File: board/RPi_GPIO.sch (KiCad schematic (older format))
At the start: 37 parts, among them IC1 ATMEGA328-A, IC2 RFM69HW, J1 RPi_GPIO, P1 FTDI_CONN_01X06, P10 SW_CONN, P11 BATT_IN, P12 CONN_01X01, P2 D4, P3 ADC0, P4 ADC1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

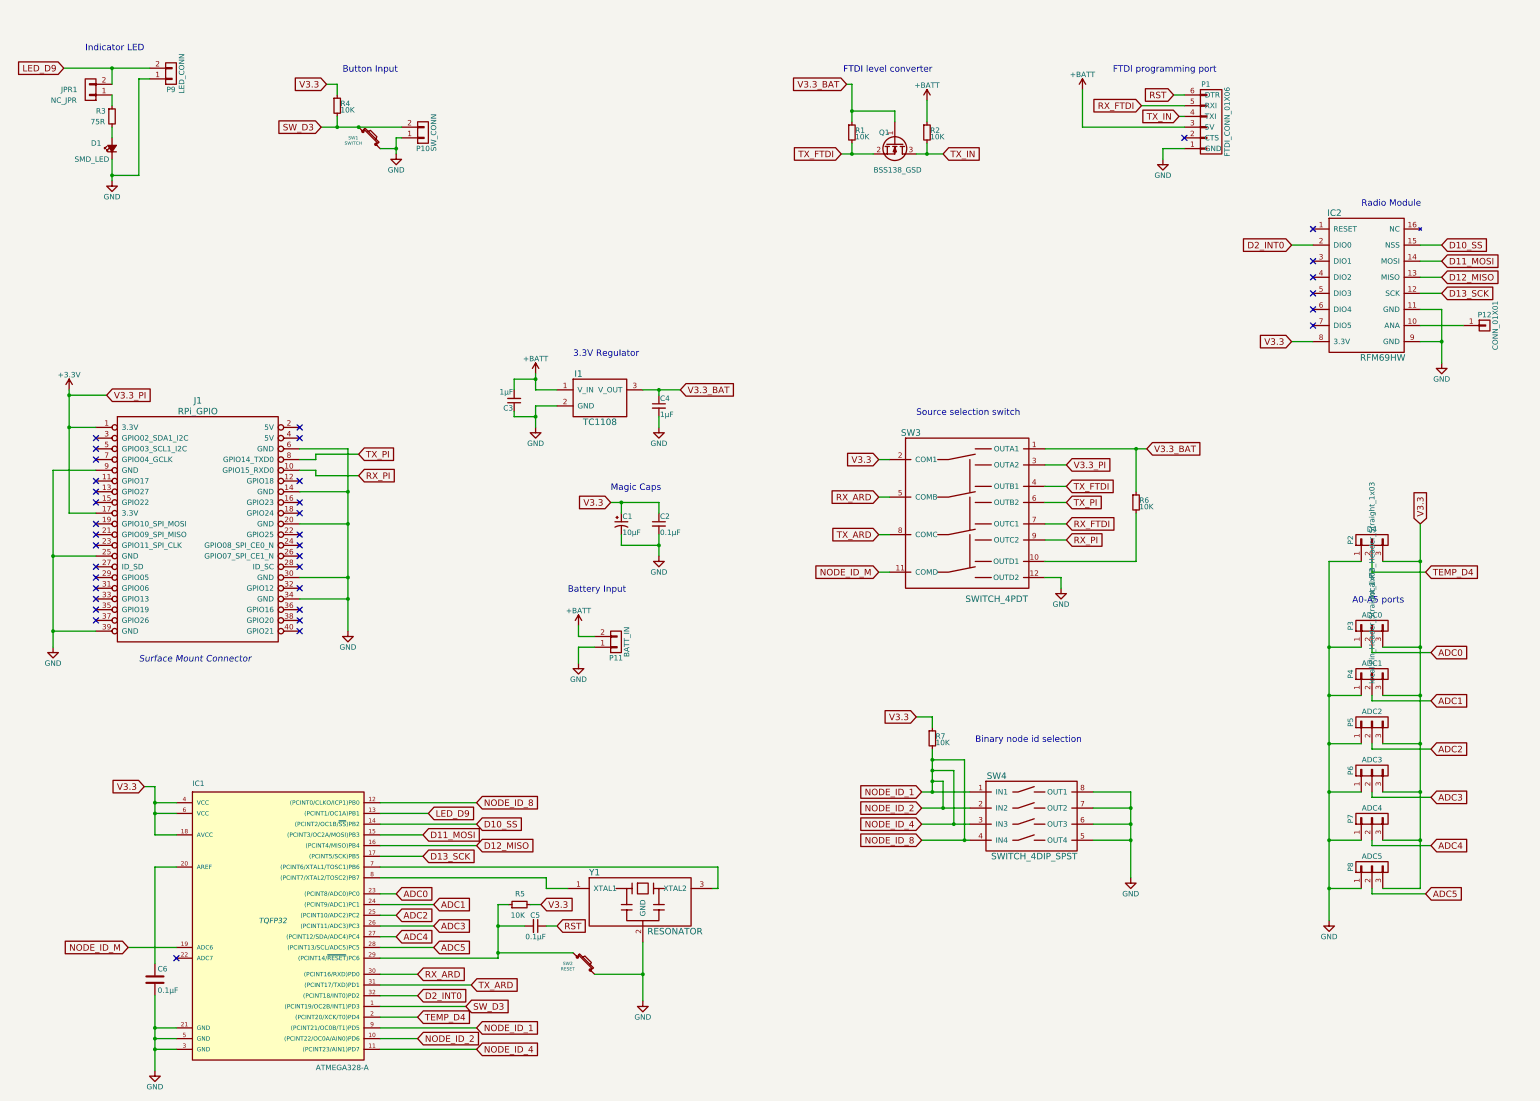
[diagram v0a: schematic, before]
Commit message: ISCP header and footprint assignments
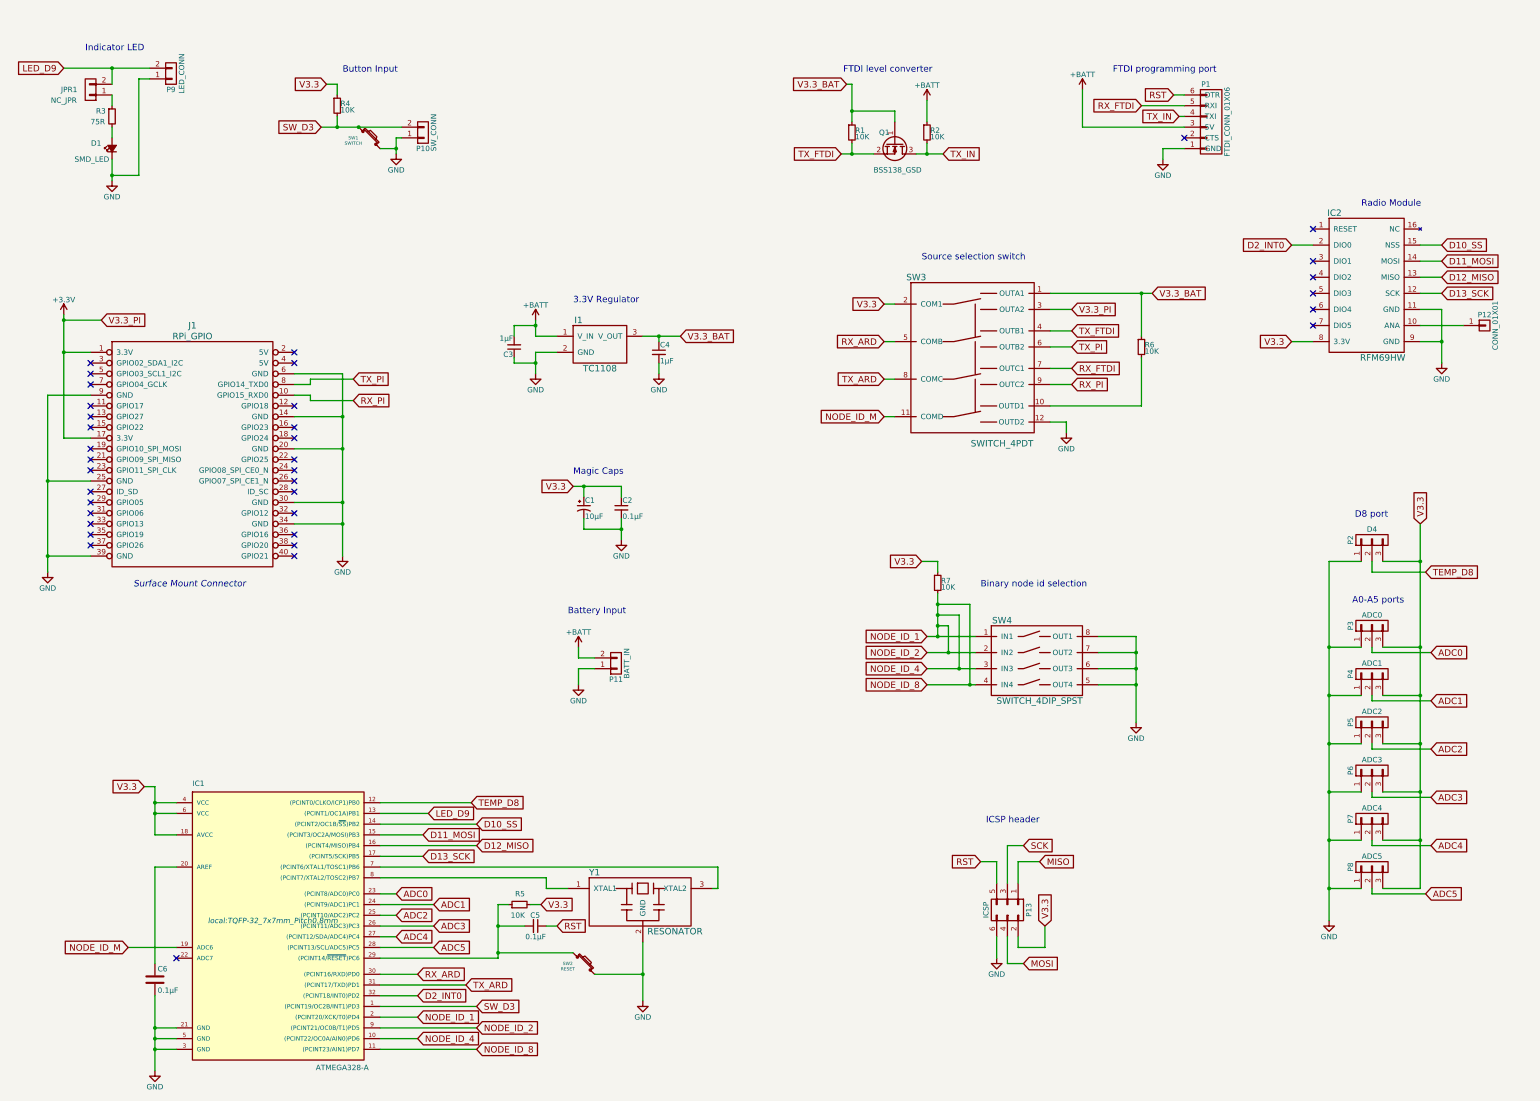
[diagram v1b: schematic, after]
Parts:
- added P13: ICSP, local:ISCP_header, symbol CONN_02X03
- IC1: footprint TQFP32 -> local:TQFP-32_7x7mm_Pitch0.8mm
- P4, P5, P6, P7, P8: footprint (none) -> local:Pin_Header_Straight_1x03
- R1, R2, R4, R5: footprint Resistors_SMD:R_0805_HandSoldering -> Resistors_SMD:R_0603_HandSoldering
- R6, R7: footprint (none) -> Resistors_SMD:R_0603_HandSoldering
- SW4: footprint (none) -> local:SW_DIP_04_GULL_BINARY
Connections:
- net GND: now also P13.6 (P6)
- net NODE_ID_1: now also IC1.2 ((PCINT20/XCK/T0)PD4); no longer IC1.12 ((PCINT0/CLKO/ICP1)PB0)
- net RST: now also P13.5 (P5)
- net V3.3: now also P13.2 (P2)
- net TEMP_D4 renamed TEMP_D8
- net TEMP_D8: now also IC1.12 ((PCINT0/CLKO/ICP1)PB0); no longer IC1.2 ((PCINT20/XCK/T0)PD4)
- new net MISO: P13.1 (P1)
- new net MOSI: P13.4 (P4)
- new net SCK: P13.3 (P3)
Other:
- note added: "D8 port"
- note added: "ICSP header"
- moved on the sheet: C1, C2, C3, C4, I1, J1, P11, R6, R7, SW3, SW4

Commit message: fixed some old (out of date) footprint assignments
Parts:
- C1: footprint Capacitors_SMD:c_elec_4x4.5 -> local:c_elec_3x5.3
- D1: footprint LEDs:LED-1206 -> LEDs:LED_1206
- I1: footprint TO_SOT_Packages_SMD:SOT-223 -> TO_SOT_Packages_SMD:SOT-23_Handsoldering
- J1: footprint RPi_Hat:Samtec_HLE-120-02-XXX-DV-BE-XX-XX -> cloudmaker:Samtec_HLE-120-02-XXX-DV-BE-XX-XX
- SW1, SW2: footprint Buttons_Switches_ThroughHole:SW_PUSH -> local:KSEx00G_SW
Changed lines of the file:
@@
 F 0 "J1" H 3300 4050 60  0000 C CNN
 F 1 "RPi_GPIO" H 3300 3950 60  0000 C CNN
-F 2 "RPi_Hat:Samtec_HLE-120-02-XXX-DV-BE-XX-XX" H 2550 3800 60  0001 C CNN
+F 2 "cloudmaker:Samtec_HLE-120-02-XXX-DV-BE-XX-XX" H 2550 3800 60  0001 C CNN
 F 3 "" H 2550 3800 60  0000 C CNN
 F 4 "~" H 2550 3800 60  0001 C CNN "Characteristics"
@@
 F 0 "I1" H 6900 3800 60  0000 C CNN
 F 1 "TC1108" H 7100 3350 60  0000 C CNN
-F 2 "TO_SOT_Packages_SMD:SOT-223" H 7000 3600 60  0001 C CNN
+F 2 "TO_SOT_Packages_SMD:SOT-23_Handsoldering" H 7000 3600 60  0001 C CNN
 F 3 "" H 7000 3600 60  0000 C CNN
 	1    7100 3650
@@
 F 0 "C1" H 6960 5320 50  0000 L CNN
 F 1 "10µF" H 6960 5170 50  0000 L CNN
-F 2 "Capacitors_SMD:c_elec_4x4.5" H 6950 5250 60  0001 C CNN
+F 2 "local:c_elec_3x5.3" H 6950 5250 60  0001 C CNN
 F 3 "" H 6950 5250 60  0000 C CNN
 	1    6950 5250
@@
 F 0 "D1" V 2600 2000 50  0000 L CNN
 F 1 "SMD_LED" V 2450 2250 50  0000 R CNN
-F 2 "LEDs:LED-1206" V 2550 1900 60  0001 C CNN
+F 2 "LEDs:LED_1206" V 2550 1900 60  0001 C CNN
 F 3 "" V 2550 1900 60  0000 C CNN
 	1    2550 1900
@@
 F 0 "SW1" H 4800 1800 30  0000 C CNN
 F 1 "SWITCH" H 4800 1750 30  0000 C CNN
-F 2 "Buttons_Switches_ThroughHole:SW_PUSH" H 4950 1800 60  0001 C CNN
+F 2 "local:KSEx00G_SW" H 4950 1800 60  0001 C CNN
 F 3 "" H 4950 1800 60  0000 C CNN
 	1    4950 1800
@@
 F 0 "SW2" H 6800 9500 30  0000 C CNN
 F 1 "RESET" H 6800 9450 30  0000 C CNN
-F 2 "Buttons_Switches_ThroughHole:SW_PUSH" H 6950 9500 60  0001 C CNN
+F 2 "local:KSEx00G_SW" H 6950 9500 60  0001 C CNN
 F 3 "" H 6950 9500 60  0000 C CNN
 	1    6950 9500

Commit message: corrections to netlist
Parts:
- added R10, R8, R9: 10K, Resistors_SMD:R_0603_HandSoldering, symbol R_Small
- JPR1: footprint Pin_Headers:Pin_Header_Straight_1x02 -> local:NC_SMD_JPR
- P2: value D4 -> D8
- P3: value ADC0 -> A0
- P4: value ADC1 -> A1
- P5: value ADC2 -> A2
- P6: value ADC3 -> A3
- P7: value ADC4 -> A4
- P8: value ADC5 -> A5
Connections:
- net MISO is gone; now on net D12_MISO: P13.1 (P1)
- net MOSI is gone; now on net D11_MOSI: P13.4 (P4)
- net SCK is gone; now on net D13_SCK: P13.3 (P3)
- net +BATT: now also P13.2 (P2)
- net NODE_ID_1: no longer IC1.10 ((PCINT22/OC0A/AIN0)PD6), IC1.11 ((PCINT23/AIN1)PD7), IC1.9 ((PCINT21/OC0B/T1)PD5), SW4.2 (IN2), SW4.3 (IN3), SW4.4 (IN4)
- net RST: now also C5.2, IC1.29 ((PCINT14/~RESET~)PC6), R5.1; no longer C5.1, P1.6 (DTR)
- net V3.3: now also R10.1, R8.1, R9.1; no longer P13.2 (P2)
- new net: C5.1, P1.6 (DTR), SW2.1
- new net NODE_ID_2: IC1.9 ((PCINT21/OC0B/T1)PD5), R8.2, SW4.2 (IN2)
- new net NODE_ID_4: IC1.10 ((PCINT22/OC0A/AIN0)PD6), R9.2, SW4.3 (IN3)
- new net NODE_ID_8: IC1.11 ((PCINT23/AIN1)PD7), R10.2, SW4.4 (IN4)
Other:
- moved on the sheet: C5, R5, R7, SW2
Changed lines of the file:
@@
 	1    0    0    1
 $EndComp
-Text GLabel 12450 1400 0    60   Input ~ 0
+Text GLabel 11600 900  0    60   Input ~ 0
 RST
 Text GLabel 12150 1500 0    60   Input ~ 0
@@
 L GND #PWR06
 U 1 1 560D33D7
-P 12350 2000
-F 0 "#PWR06" H 12350 1750 50  0001 C CNN
-F 1 "GND" H 12350 1850 50  0000 C CNN
-F 2 "" H 12350 2000 60  0000 C CNN
-F 3 "" H 12350 2000 60  0000 C CNN
-	1    12350 2000
+P 12350 2250
+F 0 "#PWR06" H 12350 2000 50  0001 C CNN
+F 1 "GND" H 12350 2100 50  0000 C CNN
+F 2 "" H 12350 2250 60  0000 C CNN
+F 3 "" H 12350 2250 60  0000 C CNN
+	1    12350 2250
 	1    0    0    -1
 $EndComp
@@
 	1    0    0    -1
 $EndComp
-Text Notes 12850 1200 2    60   ~ 0
+Text Notes 12850 700  2    60   ~ 0
 FTDI programming port
 $Comp
@@
 L GND #PWR013
 U 1 1 560D7358
-P 7500 9850
-F 0 "#PWR013" H 7500 9600 50  0001 C CNN
-F 1 "GND" H 7500 9700 50  0000 C CNN
-F 2 "" H 7500 9850 60  0000 C CNN
-F 3 "" H 7500 9850 60  0000 C CNN
-	1    7500 9850
+P 7500 9400
+F 0 "#PWR013" H 7500 9150 50  0001 C CNN
+F 1 "GND" H 7500 9250 50  0000 C CNN
+F 2 "" H 7500 9400 60  0000 C CNN
+F 3 "" H 7500 9400 60  0000 C CNN
+	1    7500 9400
 	1    0    0    -1
 $EndComp
@@
 L R_Small R5
 U 1 1 560D77C5
-P 6350 8950
-F 0 "R5" V 6450 8900 50  0000 L CNN
-F 1 "10K" V 6250 8900 50  0000 L CNN
-F 2 "Resistors_SMD:R_0603_HandSoldering" H 6350 8950 60  0001 C CNN
-F 3 "" H 6350 8950 60  0000 C CNN
-	1    6350 8950
+P 6350 9100
+F 0 "R5" V 6450 9050 50  0000 L CNN
+F 1 "10K" V 6250 9050 50  0000 L CNN
+F 2 "Resistors_SMD:R_0603_HandSoldering" H 6350 9100 60  0001 C CNN
+F 3 "" H 6350 9100 60  0000 C CNN
+	1    6350 9100
 	0    -1   -1   0
 $EndComp
-Text GLabel 6550 8950 2    60   Input ~ 0
+Text GLabel 6550 9100 2    60   Input ~ 0
 V3.3
 $Comp
@@
 F 0 "JPR1" H 2550 1350 50  0000 C CNN
 F 1 "NC_JPR" H 2600 1450 50  0000 C CNN
-F 2 "Pin_Headers:Pin_Header_Straight_1x02" H 2350 1350 60  0001 C CNN
+F 2 "local:NC_SMD_JPR" H 2350 1350 60  0001 C CNN
 F 3 "" H 2350 1350 60  0000 C CNN
 	1    2350 1350
@@
 L C_Small C5
 U 1 1 560D3E2E
-P 6500 9150
-F 0 "C5" V 6400 9100 50  0000 L CNN
-F 1 "0.1µF" V 6600 9150 50  0000 C CNN
-F 2 "Capacitors_SMD:C_0805_HandSoldering" H 6500 9150 60  0001 C CNN
-F 3 "" H 6500 9150 60  0000 C CNN
-	1    6500 9150
+P 11850 900
+F 0 "C5" V 11750 850 50  0000 L CNN
+F 1 "0.1µF" V 11950 900 50  0000 C CNN
+F 2 "Capacitors_SMD:C_0805_HandSoldering" H 11850 900 60  0001 C CNN
+F 3 "" H 11850 900 60  0000 C CNN
+	1    11850 900
 	0    1    1    0
 $EndComp
-Text GLabel 6700 9150 2    60   Input ~ 0
+Text GLabel 6450 9450 2    60   Input ~ 0
 RST
 $Comp
 L SW_PUSH_SMALL SW2
 U 1 1 577BB381
-P 6950 9500
-F 0 "SW2" H 6800 9500 30  0000 C CNN
-F 1 "RESET" H 6800 9450 30  0000 C CNN
-F 2 "local:KSEx00G_SW" H 6950 9500 60  0001 C CNN
-F 3 "" H 6950 9500 60  0000 C CNN
-	1    6950 9500
+P 13300 1000
+F 0 "SW2" H 13150 1000 30  0000 C CNN
+F 1 "RESET" H 13150 950 30  0000 C CNN
+F 2 "local:KSEx00G_SW" H 13300 1000 60  0001 C CNN
+F 3 "" H 13300 1000 60  0000 C CNN
+	1    13300 1000
 	1    0    0    -1
 $EndComp
@@
 P 14300 6350
 F 0 "P3" H 14300 6550 50  0000 C CNN
-F 1 "ADC0" V 14400 6350 50  0000 C CNN
+F 1 "A0" V 14400 6350 50  0000 C CNN
 F 2 "local:Pin_Header_Straight_1x03" H 14300 6350 50  0001 C CNN
 F 3 "" H 14300 6350 50  0000 C CNN
@@
 P 14300 6800
 F 0 "P4" H 14300 7000 50  0000 C CNN
-F 1 "ADC1" V 14400 6800 50  0000 C CNN
+F 1 "A1" V 14400 6800 50  0000 C CNN
 F 2 "local:Pin_Header_Straight_1x03" H 14300 6800 50  0001 C CNN
 F 3 "" H 14300 6800 50  0000 C CNN
@@
 P 14300 7250
 F 0 "P5" H 14300 7450 50  0000 C CNN
-F 1 "ADC2" V 14400 7250 50  0000 C CNN
+F 1 "A2" V 14400 7250 50  0000 C CNN
 F 2 "local:Pin_Header_Straight_1x03" H 14300 7250 50  0001 C CNN
 F 3 "" H 14300 7250 50  0000 C CNN
@@
 P 14300 7700
 F 0 "P6" H 14300 7900 50  0000 C CNN
-F 1 "ADC3" V 14400 7700 50  0000 C CNN
+F 1 "A3" V 14400 7700 50  0000 C CNN
 F 2 "local:Pin_Header_Straight_1x03" H 14300 7700 50  0001 C CNN
 F 3 "" H 14300 7700 50  0000 C CNN
@@
 P 14300 8150
 F 0 "P7" H 14300 8350 50  0000 C CNN
-F 1 "ADC4" V 14400 8150 50  0000 C CNN
+F 1 "A4" V 14400 8150 50  0000 C CNN
 F 2 "local:Pin_Header_Straight_1x03" H 14300 8150 50  0001 C CNN
 F 3 "" H 14300 8150 50  0000 C CNN
@@
 P 14300 8600
 F 0 "P8" H 14300 8800 50  0000 C CNN
-F 1 "ADC5" V 14400 8600 50  0000 C CNN
+F 1 "A5" V 14400 8600 50  0000 C CNN
 F 2 "local:Pin_Header_Straight_1x03" H 14300 8600 50  0001 C CNN
 F 3 "" H 14300 8600 50  0000 C CNN
@@
 P 14300 5550
 F 0 "P2" H 14300 5750 50  0000 C CNN
-F 1 "D4" V 14400 5550 50  0000 C CNN
+F 1 "D8" V 14400 5550 50  0000 C CNN
 F 2 "local:Pin_Header_Straight_1x03" H 14300 5550 50  0001 C CNN
 F 3 "" H 14300 5550 50  0000 C CNN
@@
 	12550 1900 12350 1900
 Wire Wire Line
-	12350 1900 12350 2000
+	12350 1900 12350 2250
 Wire Wire Line
 	12450 1400 12550 1400
@@
 	7650 3900 7650 4000
 Wire Wire Line
-	6550 8950 6450 8950
-Wire Wire Line
-	6250 8950 6150 8950
-Wire Wire Line
-	6150 8950 6150 9450
-Connection ~ 6150 9150
+	6550 9100 6450 9100
+Wire Wire Line
+	6250 9100 6150 9100
+Wire Wire Line
+	6150 9100 6150 9450
 Wire Wire Line
 	6850 5050 7300 5050
@@
 	5050 8500 5450 8500
 Wire Wire Line
-	6150 9450 5050 9450
+	5050 9450 6450 9450
 Wire Wire Line
 	2550 1150 2550 1300
@@
 	6600 8800 6800 8800
 Wire Wire Line
-	7500 9300 7500 9850
-Wire Wire Line
-	6600 9150 6700 9150
-Wire Wire Line
-	6150 9150 6400 9150
-Wire Wire Line
-	7050 9600 7500 9600
-Connection ~ 7500 9600
-Wire Wire Line
-	6850 9400 6150 9400
-Connection ~ 6150 9400
+	7500 9300 7500 9400
 Wire Wire Line
 	5050 8850 5200 8850
@@
 Wire Wire Line
 	9750 4400 9850 4400
-Wire Wire Line
-	10150 6450 10600 6450
-Wire Wire Line
-	10150 6600 10600 6600
-Wire Wire Line
-	10150 6750 10600 6750
-Wire Wire Line
-	10150 6900 10600 6900
-Text GLabel 10100 5750 0    60   Input ~ 0
+Text GLabel 10050 5450 0    60   Input ~ 0
 V3.3
 Wire Wire Line
-	10100 5750 10250 5750
-Wire Wire Line
-	10250 6050 10250 6450
-Connection ~ 10250 6450
-Wire Wire Line
-	10350 6600 10350 6350
-Wire Wire Line
-	10350 6350 10250 6350
-Connection ~ 10250 6350
-Connection ~ 10350 6600
-Wire Wire Line
-	10450 6750 10450 6250
-Wire Wire Line
-	10450 6250 10250 6250
-Connection ~ 10250 6250
-Connection ~ 10450 6750
-Wire Wire Line
-	10550 6900 10550 6150
-Wire Wire Line
-	10550 6150 10250 6150
-Connection ~ 10250 6150
-Connection ~ 10550 6900
+	10050 5450 10500 5450
 $Comp
 L R_Small R7
 U 1 1 577CED52
-P 10250 5950
-F 0 "R7" H 10280 5970 50  0000 L CNN
-F 1 "10K" H 10280 5910 50  0000 L CNN
-F 2 "Resistors_SMD:R_0603_HandSoldering" H 10250 5950 50  0001 C CNN
-F 3 "" H 10250 5950 50  0000 C CNN
-	1    10250 5950
-	1    0    0    -1
-$EndComp
-Wire Wire Line
-	10250 5750 10250 5850
+P 10200 5650
+F 0 "R7" H 10230 5670 50  0000 L CNN
+F 1 "10K" H 10230 5610 50  0000 L CNN
+F 2 "Resistors_SMD:R_0603_HandSoldering" H 10200 5650 50  0001 C CNN
+F 3 "" H 10200 5650 50  0000 C CNN
+	1    10200 5650
+	1    0    0    -1
+$EndComp
+Wire Wire Line
+	10200 5450 10200 5550
 $Comp
 L GND #PWR020
@@
 	11750 6900 12100 6900
 Connection ~ 12100 6900
-Text Notes 10650 6000 0    60   ~ 0
+Text Notes 10850 6000 0    60   ~ 0
 Binary node id selection
 Text Notes 14450 5350 2    60   ~ 0
@@
 $EndComp
 Text GLabel 11200 8550 2    60   Input ~ 0
-MISO
+D12_MISO
 Text GLabel 11050 8400 2    60   Input ~ 0
-SCK
+D13_SCK
 Text GLabel 10650 8550 0    60   Input ~ 0
 RST
 Text GLabel 11050 9500 2    60   Input ~ 0
-MOSI
-Text GLabel 11250 9150 1    60   Input ~ 0
-V3.3
+D11_MOSI
 $Comp
 L GND #PWR021
@@
 	10900 9500 10900 9250
 Wire Wire Line
-	11250 9150 11250 9350
-Wire Wire Line
-	11250 9350 11000 9350
+	11400 9150 11400 9350
+Wire Wire Line
+	11400 9350 11000 9350
 Wire Wire Line
 	11000 9350 11000 9250
 Text Notes 10700 8200 0    60   ~ 0
 ICSP header
+Wire Wire Line
+	10150 6450 10600 6450
+Wire Wire Line
+	10150 6600 10600 6600
+Wire Wire Line
+	10150 6750 10600 6750
+Wire Wire Line
+	10150 6900 10600 6900
+$Comp
+L R_Small R8
+U 1 1 577D2CF7
+P 10300 5850
+F 0 "R8" H 10330 5870 50  0000 L CNN
+F 1 "10K" H 10330 5810 50  0000 L CNN
+F 2 "Resistors_SMD:R_0603_HandSoldering" H 10300 5850 50  0001 C CNN
+F 3 "" H 10300 5850 50  0000 C CNN
+	1    10300 5850
+	1    0    0    -1
+$EndComp
+$Comp
+L R_Small R9
+U 1 1 577D2D88
+P 10400 6050
+F 0 "R9" H 10430 6070 50  0000 L CNN
+F 1 "10K" H 10430 6010 50  0000 L CNN
+F 2 "Resistors_SMD:R_0603_HandSoldering" H 10400 6050 50  0001 C CNN
+F 3 "" H 10400 6050 50  0000 C CNN
+	1    10400 6050
+	1    0    0    -1
+$EndComp
+$Comp
+L R_Small R10
+U 1 1 577D2F6E
+P 10500 6250
+F 0 "R10" H 10530 6270 50  0000 L CNN
+F 1 "10K" H 10530 6210 50  0000 L CNN
+F 2 "Resistors_SMD:R_0603_HandSoldering" H 10500 6250 50  0001 C CNN
+F 3 "" H 10500 6250 50  0000 C CNN
+	1    10500 6250
+	1    0    0    -1
+$EndComp
+Wire Wire Line
+	10200 5750 10200 6450
+Connection ~ 10200 6450
+Wire Wire Line
+	10300 5950 10300 6600
+Connection ~ 10300 6600
+Wire Wire Line
+	10400 6150 10400 6750
+Connection ~ 10400 6750
+Wire Wire Line
+	10500 6350 10500 6900
+Connection ~ 10500 6900
+Wire Wire Line
+	10300 5450 10300 5750
+Connection ~ 10200 5450
+Wire Wire Line
+	10400 5450 10400 5950
+Connection ~ 10300 5450
+Wire Wire Line
+	10500 5450 10500 6150
+Connection ~ 10400 5450
+$Comp
+L +BATT #PWR022
+U 1 1 577D426D
+P 11400 9150
+F 0 "#PWR022" H 11400 9000 50  0001 C CNN
+F 1 "+BATT" H 11400 9290 50  0000 C CNN
+F 2 "" H 11400 9150 60  0000 C CNN
+F 3 "" H 11400 9150 60  0000 C CNN
+	1    11400 9150
+	1    0    0    -1
+$EndComp
+Wire Wire Line
+	12450 1400 12450 900
+Wire Wire Line
+	11950 900  13200 900
+Wire Wire Line
+	11750 900  11600 900
+Connection ~ 12450 900
+Wire Wire Line
+	13400 1100 13400 2100
+Wire Wire Line
+	13400 2100 12350 2100
+Connection ~ 12350 2100
+Connection ~ 6150 9450
 $EndSCHEMATC
